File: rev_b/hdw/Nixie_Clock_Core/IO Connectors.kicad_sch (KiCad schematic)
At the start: 4 parts, among them J1901 Conn_02x32_Top_Bottom

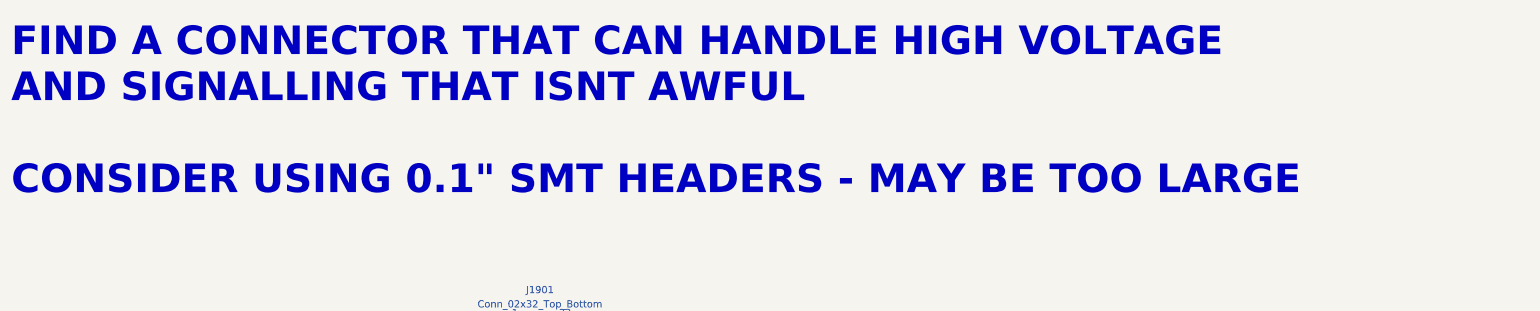
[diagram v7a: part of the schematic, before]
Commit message: added BOM for IN12 carrier, finished routing, some schematic tweaks, adjusted design rules for ERC
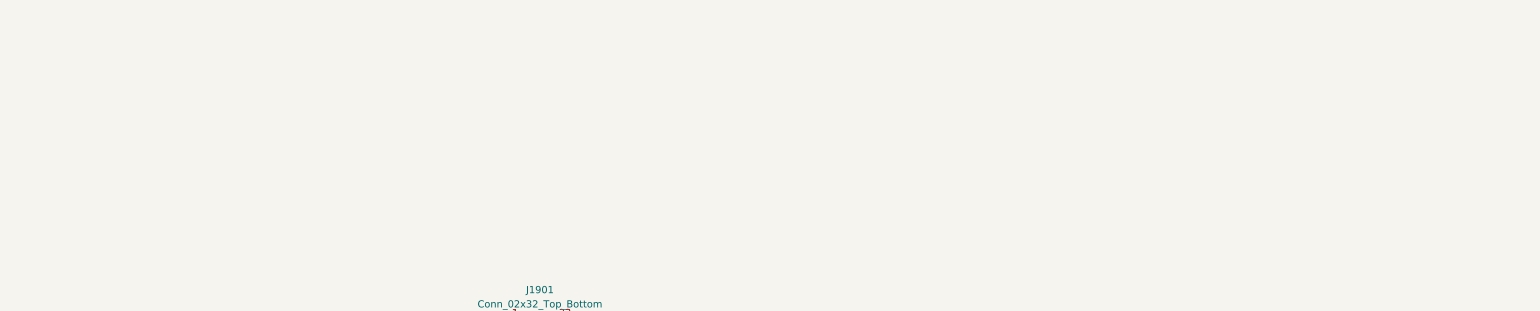
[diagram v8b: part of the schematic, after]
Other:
- note removed: "FIND A CONNECTOR THAT CAN HANDLE HIGH VOLTAGE AND SIGNALLING THAT ISNT AWFUL CONSIDER USING 0.1" SMT HEADERS - MAY BE TOO LARGE"
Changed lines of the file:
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@@
   (no_connect (at 124.46 74.93))
   (no_connect (at 124.46 82.55))
-  (text "FIND A CONNECTOR THAT CAN HANDLE HIGH VOLTAGE\nAND SIGNALLING THAT ISNT AWFUL\n\nCONSIDER USING 0.1\" SMT HEADERS - MAY BE TOO LARGE"
-    (at 36.83 48.26 0)
-    (effects (font (face "Courier New") (size 5.08 5.08) (thickness 0.254) bold (color 255 37 56 1)) (justify left bottom))
-  )
   (global_label "Colon_3_DSP" (shape input) (at 137.16 115.57 0) (fields_autoplaced)
     (effects (font (size 1.27 1.27)) (justify left))
